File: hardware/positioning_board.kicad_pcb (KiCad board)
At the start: 2 copper layers, 29 parts, among them J1 4P4C, J2 USB_C_Receptacle_USB2.0_16P, J3 Conn_01x04, J4 Conn_01x05, J5 Conn_01x05, Q1 MMBT3904, Q2 MMBT3904, SW1 SW_Push, SW2 SW_Push, U1 SN65HVD1782DR, U2 CH340K, U3 ESP32-S3-WROOM-1, U4 LSM6DS3

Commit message: feat: draft layout
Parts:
- added C10: 100n, Capacitor_SMD:C_0603_1608Metric, F.Cu at (153.9, 75.0)
- added C11: 22u, Capacitor_SMD:C_0603_1608Metric, F.Cu at (150.2, 74.0)
- added C12: 22u, Capacitor_SMD:C_0603_1608Metric, F.Cu at (148.7, 74.0)
- added C13: 10u, Capacitor_SMD:C_0603_1608Metric, F.Cu at (161.2, 74.7)
- added C14: 22u, Capacitor_SMD:C_0603_1608Metric, F.Cu at (163.7, 74.7)
- added C7: 100n, Capacitor_SMD:C_0603_1608Metric, F.Cu at (155.3, 82.1)
- added C8: 10u, Capacitor_SMD:C_0603_1608Metric, F.Cu at (149.5, 77.0)
- added C9: 10u, Capacitor_SMD:C_0603_1608Metric, F.Cu at (149.5, 78.5)
- added D1: SS24, Diode_SMD:D_SMA, F.Cu at (120.5, 84.0)
- added D2: SS24, Diode_SMD:D_SMA, F.Cu at (131.0, 73.5)
- added H1: MountingHole, MountingHole:MountingHole_3.2mm_M3, F.Cu at (175.0, 95.5)
- added L1: 3.3u, Inductor_SMD:L_Changjiang_FXL0630, F.Cu at (142.2, 76.0)
- added R11: 10k, Resistor_SMD:R_0603_1608Metric, F.Cu at (158.2, 77.7)
- added R12: 56.2k, Resistor_SMD:R_0603_1608Metric, F.Cu at (156.7, 77.7)
- added U5: TPS563200, Package_TO_SOT_SMD:SOT-23-6, F.Cu at (153.6, 77.5)
- added U7: AMS1117-3.3, Package_TO_SOT_SMD:SOT-223-3_TabPin2, F.Cu at (163.7, 81.0)
- moved J4 97.2 mm to (171.5, 86.0), turned to 90 degrees
- moved J1 64.1 mm to (163.0, 93.5), turned to 180 degrees
- moved C3 62.4 mm to (152.0, 98.3), turned to 90 degrees
- moved C4 61.3 mm to (154.0, 98.3), turned to -90 degrees
- moved Q1 57.8 mm to (126.9, 98.0)
- moved R1 57.6 mm to (123.5, 97.0)
- moved R2 57.0 mm to (123.5, 99.0), turned to 180 degrees
- moved R10 54.7 mm to (152.7, 96.0), turned to 180 degrees
- moved C1 54.7 mm to (124.3, 94.0)
- moved Q2 54.4 mm to (120.0, 98.0), turned to 180 degrees
- moved R9 52.5 mm to (152.7, 91.0)
- moved U3 52.2 mm to (139.9, 89.9), turned to 180 degrees
- moved R4 50.4 mm to (116.7, 96.8)
- moved R3 48.4 mm to (116.7, 92.2)
- moved C2 45.2 mm to (124.3, 87.0), turned to 180 degrees
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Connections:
- J1 pad 1: unconnected-(J1-Pad1) -> /A
- J1 pad 2: unconnected-(J1-Pad2) -> /B
- J1 pad 3: unconnected-(J1-Pad3) -> GND
- J1 pad 4: unconnected-(J1-Pad4) -> +12V
- J2 pad A4: +5V -> Net-(D1-A)
- J2 pad A9: +5V -> Net-(D1-A)
- J2 pad B4: +5V -> Net-(D1-A)
- J2 pad B9: +5V -> Net-(D1-A)
- J5 pad 4: /Encoder1_X -> /Encoder2_X
- R7 pad 2: +3V3D -> +3V3
- R9 pad 2: +3V3D -> +3V3
- U1 pad 1: unconnected-(U1-R-Pad1) -> /Brain_RX
- U1 pad 2: unconnected-(U1-~{RE}-Pad2) -> /Brain_Dir
- U1 pad 3: unconnected-(U1-DE-Pad3) -> /Brain_Dir
- U1 pad 4: unconnected-(U1-D-Pad4) -> /Brain_TX
- U1 pad 5: unconnected-(U1-GND-Pad5) -> GND
- U1 pad 6: unconnected-(U1-A-Pad6) -> /A
- U1 pad 7: unconnected-(U1-B-Pad7) -> /B
- U1 pad 8: unconnected-(U1-VCC-Pad8) -> +3V3
- U3 pad 10: unconnected-(U3-IO17-Pad10) -> /Brain_TX
- U3 pad 11: unconnected-(U3-IO18-Pad11) -> /Brain_RX
- U3 pad 12: unconnected-(U3-IO8-Pad12) -> /Brain_Dir
- U3 pad 18: unconnected-(U3-IO10-Pad18) -> /IMU_CS
- U3 pad 19: unconnected-(U3-IO11-Pad19) -> /IMU_In
- U3 pad 20: unconnected-(U3-IO12-Pad20) -> /IMU_CLK
- U3 pad 21: unconnected-(U3-IO13-Pad21) -> /IMU_Out
- U3 pad 24: unconnected-(U3-IO47-Pad24) -> /LIDAR_RX
- U3 pad 25: unconnected-(U3-IO48-Pad25) -> /LIDAR_PWM
- U3 pad 31: unconnected-(U3-IO38-Pad31) -> /Encoder2_B
- U3 pad 32: unconnected-(U3-IO39-Pad32) -> /Encoder2_A
- U3 pad 33: unconnected-(U3-IO40-Pad33) -> /Encoder2_X
- U3 pad 7: unconnected-(U3-IO7-Pad7) -> /Encoder1_B
- U3 pad 8: unconnected-(U3-IO15-Pad8) -> /Encoder1_A
- U3 pad 9: unconnected-(U3-IO16-Pad9) -> /Encoder1_X
- U4 pad 12: GND -> /IMU_CS
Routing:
- net +3V3: track 0.00 -> 98.1 mm, vias 0 -> 9
- net +5V: track 0.00 -> 85.9 mm, vias 0 -> 3
- net GND: track 0.00 -> 57.1 mm, vias 0 -> 14
- net +12V: track 0.00 -> 53.7 mm
- net /GPIO0: track 0.00 -> 32.1 mm, vias 0 -> 2
- net /Encoder1_B: track 0.00 -> 32.0 mm
- net /MCU_EN: track 0.00 -> 30.8 mm
- net /Encoder1_X: track 0.00 -> 30.3 mm
- net /Encoder1_A: track 0.00 -> 29.8 mm
- net Net-(D2-A): track 0.00 -> 28.0 mm, vias 0 -> 2
- net /Encoder2_B: track 0.00 -> 22.8 mm
- net Net-(D1-A): track 0.00 -> 20.1 mm, vias 0 -> 2
- net /Encoder2_A: track 0.00 -> 18.6 mm
- net /Encoder2_X: track 0.00 -> 18.4 mm
- net /LIDAR_RX: track 0.00 -> 17.1 mm
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- added copper zone on B.Cu, net GND
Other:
- board outline added: 75 x 32 mm

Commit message: reroute lidar pins
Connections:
- U3 pad 24: /LIDAR_RX -> unconnected-(U3-IO47-Pad24)
- U3 pad 25: /LIDAR_PWM -> unconnected-(U3-IO48-Pad25)
- U3 pad 38: unconnected-(U3-IO2-Pad38) -> /LIDAR_PWM
- U3 pad 39: unconnected-(U3-IO1-Pad39) -> /LIDAR_RX
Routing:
- net /LIDAR_RX: track 17.1 -> 31.3 mm, vias 0 -> 2
- net /LIDAR_PWM: track 16.8 -> 29.7 mm, vias 0 -> 2
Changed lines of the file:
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@@
 	(net 48 "unconnected-(U3-IO21-Pad23)")
 	(net 49 "unconnected-(U3-IO9-Pad17)")
-	(net 50 "unconnected-(U3-IO2-Pad38)")
+	(net 50 "unconnected-(U3-IO47-Pad24)")
 	(net 51 "unconnected-(U3-USB_D+-Pad14)")
 	(net 52 "unconnected-(U3-IO37-Pad30)")
@@
 	(net 55 "unconnected-(U3-IO5-Pad5)")
 	(net 56 "unconnected-(U3-IO6-Pad6)")
-	(net 57 "unconnected-(U3-IO1-Pad39)")
+	(net 57 "unconnected-(U3-IO48-Pad25)")
 	(net 58 "unconnected-(U3-IO45-Pad26)")
 	(net 59 "unconnected-(U3-IO4-Pad4)")
@@
 			(size 1.5 0.9)
 			(layers "F.Cu" "F.Mask" "F.Paste")
-			(net 2 "/LIDAR_RX")
+			(net 50 "unconnected-(U3-IO47-Pad24)")
 			(pinfunction "IO47")
-			(pintype "bidirectional")
+			(pintype "bidirectional+no_connect")
 		)
 		(pad "25" smd rect
@@
 			(size 1.5 0.9)
 			(layers "F.Cu" "F.Mask" "F.Paste")
-			(net 1 "/LIDAR_PWM")
+			(net 57 "unconnected-(U3-IO48-Pad25)")
 			(pinfunction "IO48")
-			(pintype "bidirectional")
+			(pintype "bidirectional+no_connect")
 		)
 		(pad "26" smd rect
@@
 			(size 1.5 0.9)
 			(layers "F.Cu" "F.Mask" "F.Paste")
-			(net 50 "unconnected-(U3-IO2-Pad38)")
+			(net 1 "/LIDAR_PWM")
 			(pinfunction "IO2")
-			(pintype "bidirectional+no_connect")
+			(pintype "bidirectional")
 		)
 		(pad "39" smd rect
@@
 			(size 1.5 0.9)
 			(layers "F.Cu" "F.Mask" "F.Paste")
-			(net 57 "unconnected-(U3-IO1-Pad39)")
+			(net 2 "/LIDAR_RX")
 			(pinfunction "IO1")
-			(pintype "bidirectional+no_connect")
+			(pintype "bidirectional")
 		)
 		(pad "40" smd rect
@@
 	)
 	(segment
-		(start 127.464448 78.674)
-		(end 128.290448 79.5)
+		(start 132.5 94.73)
+		(end 131.45 95.78)
 		(width 0.3)
 		(layer "F.Cu")
@@
 	)
 	(segment
-		(start 128.290448 79.5)
-		(end 133.557 79.5)
+		(start 127.464448 78.674)
+		(end 128.145224 79.354776)
 		(width 0.3)
 		(layer "F.Cu")
@@
 	)
 	(segment
-		(start 134.185 80.128)
-		(end 134.185 80.56)
+		(start 128.145224 79.354776)
+		(end 128.290448 79.5)
 		(width 0.3)
 		(layer "F.Cu")
@@
 	)
 	(segment
+		(start 132.5 82.5)
+		(end 132.5 94.73)
+		(width 0.3)
+		(layer "F.Cu")
+		(net 1)
+	)
+	(segment
 		(start 126.009 78.674)
 		(end 127.464448 78.674)
@@
 	)
 	(segment
+		(start 131.45 95.78)
+		(end 131.15 95.78)
+		(width 0.3)
+		(layer "F.Cu")
+		(net 1)
+	)
+	(segment
 		(start 123.75 72)
 		(end 123.75 76.415)
@@
 	)
 	(segment
-		(start 133.557 79.5)
-		(end 134.185 80.128)
+		(start 128.290448 79.5)
+		(end 129.5 79.5)
 		(width 0.3)
 		(layer "F.Cu")
@@
 	)
 	(segment
+		(start 129.5 79.5)
+		(end 130.5 80.5)
+		(width 0.3)
+		(layer "F.Cu")
+		(net 1)
+	)
+	(via
+		(at 130.5 80.5)
+		(size 0.6)
+		(drill 0.3)
+		(layers "F.Cu" "B.Cu")
+		(net 1)
+	)
+	(via
+		(at 132.5 82.5)
+		(size 0.6)
+		(drill 0.3)
+		(layers "F.Cu" "B.Cu")
+		(net 1)
+	)
+	(segment
+		(start 130.5 80.5)
+		(end 132.5 82.5)
+		(width 0.3)
+		(layer "B.Cu")
+		(net 1)
+	)
+	(segment
+		(start 133.200003 95.431997)
+		(end 131.582 97.05)
+		(width 0.3)
+		(layer "F.Cu")
+		(net 2)
+	)
+	(segment
 		(start 125.25 77.3479)
 		(end 125.25 72)
@@
 	)
 	(segment
-		(start 135.455 80.128)
-		(end 135.455 80.56)
+		(start 130.099 79.099)
+		(end 131 80)
 		(width 0.3)
 		(layer "F.Cu")
@@
 	)
 	(segment
-		(start 134.426 79.099)
-		(end 135.455 80.128)
+		(start 133.200003 82.5)
+		(end 133.200003 95.431997)
 		(width 0.3)
 		(layer "F.Cu")
@@
 	)
 	(segment
-		(start 128.456548 79.099)
-		(end 134.426 79.099)
+		(start 126.1751 78.273)
+		(end 127.630548 78.273)
 		(width 0.3)
 		(layer "F.Cu")
@@
 	)
 	(segment
-		(start 126.1751 78.273)
-		(end 127.630548 78.273)
+		(start 131.582 97.05)
+		(end 131.15 97.05)
 		(width 0.3)
 		(layer "F.Cu")
@@
 		(net 2)
 	)
+	(segment
+		(start 128.456548 79.099)
+		(end 130.099 79.099)
+		(width 0.3)
+		(layer "F.Cu")
+		(net 2)
+	)
+	(via
+		(at 131 80)
+		(size 0.6)
+		(drill 0.3)
+		(layers "F.Cu" "B.Cu")
+		(net 2)
+	)
+	(via
+		(at 133.200003 82.5)
+		(size 0.6)
+		(drill 0.3)
+		(layers "F.Cu" "B.Cu")
+		(net 2)
+	)
+	(segment
+		(start 131 80)
+		(end 133.200003 82.200003)
+		(width 0.3)
+		(layer "B.Cu")
+		(net 2)
+	)
+	(segment
+		(start 133.200003 82.200003)
+		(end 133.200003 82.5)
+		(width 0.3)
+		(layer "B.Cu")
+		(net 2)
+	)

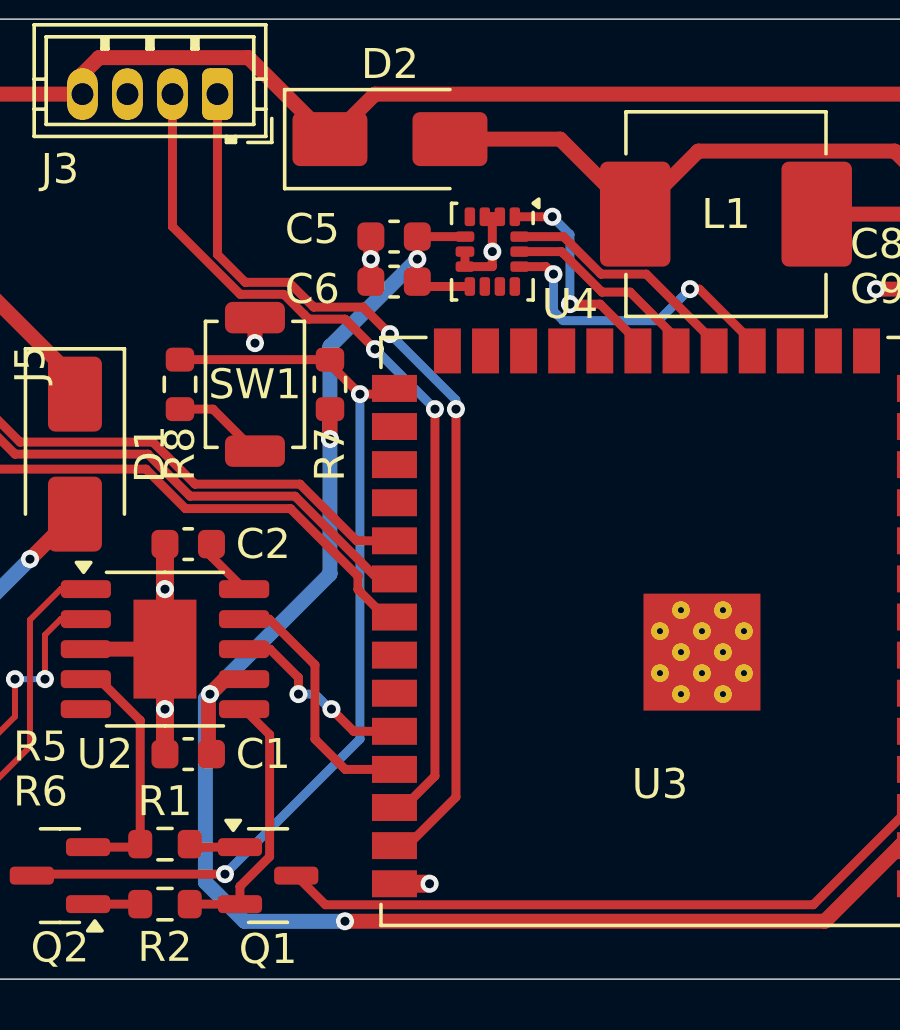
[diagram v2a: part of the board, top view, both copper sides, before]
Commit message: reroute some pins
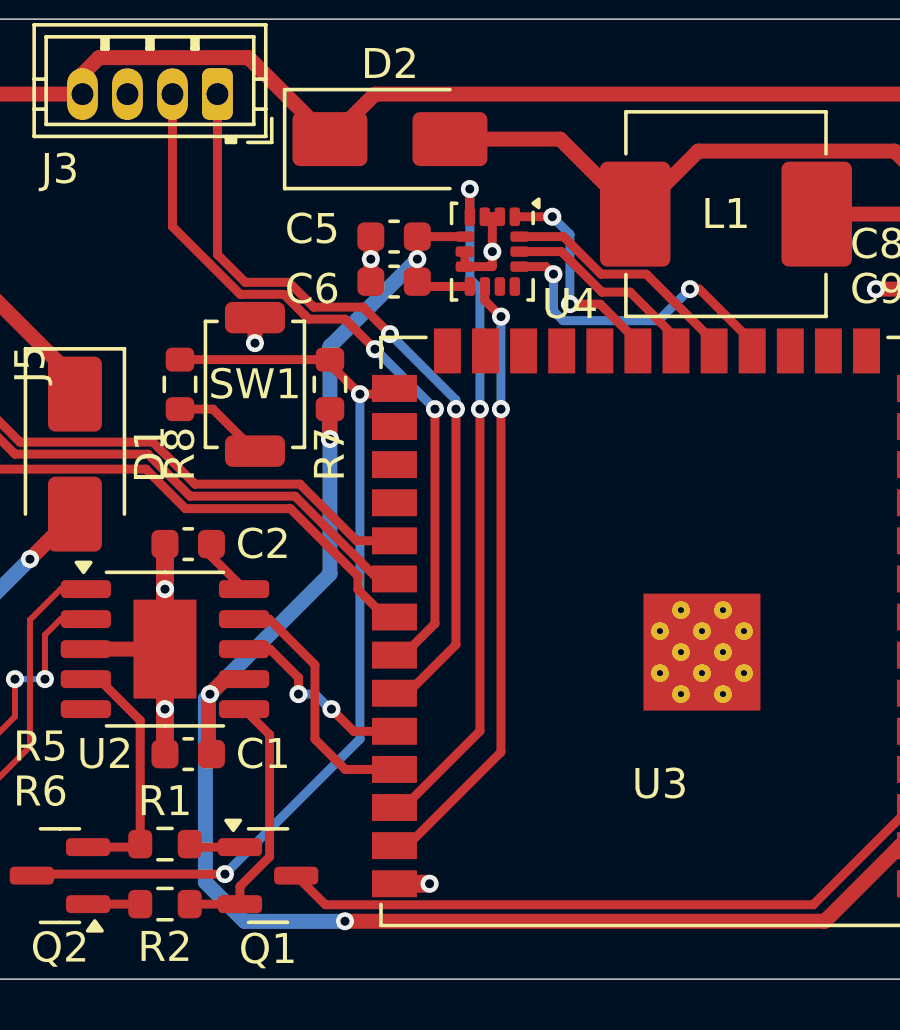
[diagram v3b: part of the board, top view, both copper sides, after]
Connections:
- U3 pad 34: unconnected-(U3-IO41-Pad34) -> /LIDAR_PWM
- U3 pad 35: unconnected-(U3-IO42-Pad35) -> /LIDAR_RX
- U3 pad 38: /LIDAR_PWM -> /IMU_INT1
- U3 pad 39: /LIDAR_RX -> /IMU_INT2
- U4 pad 4: unconnected-(U4-INT1-Pad4) -> /IMU_INT1
- U4 pad 9: unconnected-(U4-INT2-Pad9) -> /IMU_INT2
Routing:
- net /IMU_INT1: track 0.00 -> 23.0 mm, vias 0 -> 2
- net /IMU_INT2: track 0.00 -> 20.6 mm, vias 0 -> 2
- net /LIDAR_RX: track 31.3 -> 26.2 mm
- net /LIDAR_PWM: track 29.7 -> 24.6 mm

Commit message: relayout board
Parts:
- removed U7: AMS1117-3.3, Package_TO_SOT_SMD:SOT-223-3_TabPin2
- added D13: CESD3V3AP, Package_TO_SOT_SMD:SOT-23, F.Cu at (164.6, 102.5)
- added H2: MountingHole, MountingHole:MountingHole_4.3mm_M4, F.Cu at (174.0, 75.0)
- added H3: MountingHole, MountingHole:MountingHole_4.3mm_M4, F.Cu at (140.0, 105.0)
- added R13: 10k, Resistor_SMD:R_0603_1608Metric, F.Cu at (112.3, 102.5)
- added R14: 10k, Resistor_SMD:R_0603_1608Metric, F.Cu at (112.3, 106.0)
- added U6: CH340K, Package_SO:SSOP-10-1EP_3.9x4.9mm_P1mm_EP2.1x3.3mm, F.Cu at (119.3, 95.0)
- C1: value 100n -> 10u
- C13: value 10u -> 100n
- C14: value 22u -> 100n
- C2: value 100n -> 22u
- H1: footprint MountingHole:MountingHole_3.2mm_M3 -> MountingHole:MountingHole_4.3mm_M4
- J1: value 4P4C -> Conn_01x04; footprint RJ11:RJ11-4P4C -> Connector_JST:JST_ZH_B4B-ZR_1x04_P1.50mm_Vertical
- J2: value USB_C_Receptacle_USB2.0_16P -> Conn_01x05; footprint Connector_USB:USB_C_Receptacle_GCT_USB4105-xx-A_16P_TopMnt_Horizontal -> Connector_JST:JST_XH_S5B-XH-A_1x05_P2.50mm_Horizontal
- J3: value Conn_01x04 -> Conn_01x05; footprint Connector_JST:JST_ZH_B4B-ZR_1x04_P1.50mm_Vertical -> Connector_JST:JST_XH_S5B-XH-A_1x05_P2.50mm_Horizontal
- J4: value Conn_01x05 -> 4P4C; footprint Connector_JST:JST_XH_S5B-XH-A_1x05_P2.50mm_Horizontal -> RJ11:RJ11-4P4C
- J5: value Conn_01x05 -> USB_C_Receptacle_USB2.0_16P; footprint Connector_JST:JST_XH_S5B-XH-A_1x05_P2.50mm_Horizontal -> Connector_USB:USB_C_Receptacle_GCT_USB4105-xx-A_16P_TopMnt_Horizontal
- R1, R2: value 10k -> 10
- R10: value 1k -> 22
- R12: value 56.2k -> 10k
- R3, R4: value 5.1k -> 10k
- R5: value 22 -> 56.2k
- R6: value 22 -> 10k
- R7: value 10k -> 5.1k
- R8: value 1k -> 5.1k
- R9: value 10k -> 22
- U1: value SN65HVD1782DR -> AMS1117-3.3; footprint Package_SO:SOIC-8_3.9x4.9mm_P1.27mm -> Package_TO_SOT_SMD:SOT-223-3_TabPin2
- U2: value CH340K -> ESP32-S3-WROOM-1; footprint Package_SO:SSOP-10-1EP_3.9x4.9mm_P1mm_EP2.1x3.3mm -> RF_Module:ESP32-S3-WROOM-1U
- U3: value ESP32-S3-WROOM-1 -> LSM6DS3; footprint RF_Module:ESP32-S3-WROOM-1U -> Package_LGA:LGA-14_3x2.5mm_P0.5mm_LayoutBorder3x4y
- U4: value LSM6DS3 -> SN65HVD1782DR; footprint Package_LGA:LGA-14_3x2.5mm_P0.5mm_LayoutBorder3x4y -> Package_SO:SOIC-8_3.9x4.9mm_P1.27mm
- moved H1 72.0 mm to (106.0, 75.0)
- moved R5 59.2 mm to (175.1, 84.0), turned to 180 degrees
- moved R6 59.2 mm to (175.1, 85.5)
- moved J2 51.7 mm to (159.0, 77.0), turned to 180 degrees
- moved SW2 46.6 mm to (107.8, 106.0)
- moved R11 45.0 mm to (119.2, 100.0), turned to 0 degrees
- moved R12 44.7 mm to (119.2, 102.0), turned to 180 degrees
- moved C14 42.8 mm to (125.0, 93.0), turned to 0 degrees
- moved C13 42.0 mm to (125.0, 96.0), turned to 180 degrees
- moved R9 41.8 mm to (111.0, 94.0)
- moved R10 41.7 mm to (111.0, 96.0), turned to 0 degrees
- moved R1 41.6 mm to (164.3, 105.0), turned to 180 degrees
- moved R2 40.8 mm to (164.3, 100.0), turned to 0 degrees
- moved R3 38.3 mm to (154.5, 98.2), turned to 90 degrees
- moved R4 36.9 mm to (153.0, 103.3), turned to 90 degrees
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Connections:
- C1 pad 2: +3V3 -> +5V
- C11 pad 2: Net-(D2-A) -> /12V_Buck/+5V
- C12 pad 2: Net-(D2-A) -> /12V_Buck/+5V
- C13 pad 2: +5V -> +3V3
- C14 pad 1: GND -> Net-(U6-V3)
- C14 pad 2: +3V3 -> GND
- C2 pad 1: Net-(U2-V3) -> GND
- C2 pad 2: GND -> +3V3
- C7 pad 1: GND -> +3V3
- C7 pad 2: +3V3 -> GND
- C8 pad 2: +12V -> /12V_Buck/+12V
- C9 pad 2: +12V -> /12V_Buck/+12V
- D1 pad 2: Net-(D1-A) -> /usb_port/+5V
- D2 pad 2: Net-(D2-A) -> /12V_Buck/+5V
- J1 pad 1: /A -> /LIDAR_RX
- J1 pad 2: /B -> /LIDAR_PWM
- J1 pad 4: +12V -> +5V
- J3 pad 1: /LIDAR_RX -> /Encoder2_B
- J3 pad 2: /LIDAR_PWM -> +5V
- J3 pad 3: GND -> /Encoder2_A
- J3 pad 4: +5V -> /Encoder2_X
- J4 pad 1: /Encoder1_B -> /SmartPort/A
- J4 pad 2: +5V -> /SmartPort/B
- J4 pad 3: /Encoder1_A -> GND
- J4 pad 4: /Encoder1_X -> /12V_Buck/+12V
- L1 pad 2: Net-(D2-A) -> /12V_Buck/+5V
- Q1 pad 2: /RTS -> /usb_port/RTS
- Q2 pad 2: /DTR -> /usb_port/DTR
- R1 pad 1: /DTR -> /SmartPort/B
- R1 pad 2: Net-(Q1-B) -> Net-(U4-B)
- R10 pad 1: Net-(R10-Pad1) -> Net-(J5-D+-PadA6)
- R10 pad 2: /MCU_EN -> /usb_port/USB_D+
- R11 pad 1: GND -> /usb_port/DTR
- R11 pad 2: Net-(U5-VFB) -> Net-(Q1-B)
- R12 pad 1: Net-(U5-VFB) -> /usb_port/RTS
- R12 pad 2: Net-(D2-A) -> Net-(Q2-B)
- R2 pad 1: /RTS -> Net-(U4-A)
- R2 pad 2: Net-(Q2-B) -> /SmartPort/A
- R3 pad 1: Net-(J2-CC1) -> /Brain_RX
- R3 pad 2: GND -> +3V3
- R4 pad 1: Net-(J2-CC2) -> GND
- R4 pad 2: GND -> /Brain_Dir
- R5 pad 1: Net-(J2-D--PadA7) -> Net-(U5-VFB)
- R5 pad 2: /USB_D- -> /12V_Buck/+5V
- R6 pad 1: Net-(J2-D+-PadA6) -> GND
- R6 pad 2: /USB_D+ -> Net-(U5-VFB)
- R7 pad 1: /GPIO0 -> Net-(J5-CC1)
- R7 pad 2: +3V3 -> GND
- R8 pad 1: Net-(R8-Pad1) -> Net-(J5-CC2)
- R8 pad 2: /GPIO0 -> GND
- R9 pad 1: /MCU_EN -> Net-(J5-D--PadA7)
- R9 pad 2: +3V3 -> /usb_port/USB_D-
- SW1 pad 2: Net-(R8-Pad1) -> /GPIO0
- SW2 pad 2: Net-(R10-Pad1) -> /MCU_EN
- U1 pad 1: /Brain_RX -> GND
- U1 pad 2: /Brain_Dir -> +3V3
- U1 pad 3: /Brain_Dir -> +5V
- U2 pad 1: /USB_D+ -> GND
- U2 pad 10: Net-(U2-V3) -> /Brain_TX
- U2 pad 11: GND -> /Brain_RX
- U2 pad 2: /USB_D- -> +3V3
- U2 pad 3: GND -> /MCU_EN
- U2 pad 4: /DTR -> unconnected-(U2-IO4-Pad4)
- U2 pad 6: /RTS -> unconnected-(U2-IO6-Pad6)
- U2 pad 7: +3V3 -> /Encoder1_B
- U2 pad 8: /Prog_RX -> /Encoder1_A
- U2 pad 9: /Prog_TX -> /Encoder1_X
- U3 pad 1: GND -> /IMU_Out
- U3 pad 10: /Brain_TX -> unconnected-(U3-NC-Pad10)
- U3 pad 11: /Brain_RX -> unconnected-(U3-NC-Pad11)
- U3 pad 12: /Brain_Dir -> /IMU_CS
- U3 pad 13: unconnected-(U3-USB_D--Pad13) -> /IMU_CLK
- U3 pad 14: unconnected-(U3-USB_D+-Pad14) -> /IMU_In
- U3 pad 2: +3V3 -> GND
- U3 pad 3: /MCU_EN -> GND
- U3 pad 4: unconnected-(U3-IO4-Pad4) -> /IMU_INT1
- U3 pad 5: unconnected-(U3-IO5-Pad5) -> +3V3
- U3 pad 6: unconnected-(U3-IO6-Pad6) -> GND
- U3 pad 7: /Encoder1_B -> GND
- U3 pad 8: /Encoder1_A -> +3V3
- U3 pad 9: /Encoder1_X -> /IMU_INT2
- U4 pad 1: /IMU_Out -> /Brain_RX
- U4 pad 2: GND -> /Brain_Dir
- U4 pad 3: GND -> /Brain_Dir
- U4 pad 4: /IMU_INT1 -> /Brain_TX
- U4 pad 5: +3V3 -> GND
- U4 pad 6: GND -> Net-(U4-A)
- U4 pad 7: GND -> Net-(U4-B)
- U5 pad 3: +12V -> /12V_Buck/+12V
- U5 pad 5: +12V -> /12V_Buck/+12V
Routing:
- net +12V: track 53.7 -> 0.00 mm
- net Net-(D2-A): track 28.0 -> 0.00 mm, vias 2 -> 0
- net /12V_Buck/+12V: track 0.00 -> 26.5 mm
- net /Brain_Dir: track 3.95 -> 25.8 mm, vias 0 -> 2
- net Net-(D1-A): track 20.1 -> 0.00 mm, vias 2 -> 0
- net /usb_port/+5V: track 0.00 -> 19.8 mm, vias 0 -> 2
- net /Brain_TX: track 2.68 -> 21.2 mm, vias 0 -> 2
- net /Encoder1_X: track 30.3 -> 13.5 mm
- net /Encoder1_A: track 29.8 -> 15.8 mm
- net /Encoder1_B: track 32.0 -> 19.1 mm
- net /MCU_EN: track 30.8 -> 42.9 mm
- net /A: track 11.7 -> 0.00 mm
- net /Encoder2_B: track 22.8 -> 11.4 mm
- net Net-(U5-SW): track 11.3 -> 0.00 mm, vias 0 -> 7
- net /Brain_RX: track 8.19 -> 18.4 mm, vias 0 -> 2
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- added copper zone on F.Cu, net +3V3
- added copper zone on F.Cu, net /12V_Buck/+12V
- added copper zone on F.Cu, net /12V_Buck/+5V
- added copper zone on F.Cu, net GND
- added copper zone on B.Cu, net Net-(U5-SW)
- added copper zone on F.Cu, net Net-(U5-SW)
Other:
- board size 75 x 32 mm -> 83 x 43 mm
- board text added: "BOOT"
- board text added: "Buck"
- board text added: "EN"
- board text added: "Programmer"
- board text added: "Smart Port"
